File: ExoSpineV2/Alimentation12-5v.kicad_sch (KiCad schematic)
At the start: 8 parts, among them U5 TPS564247

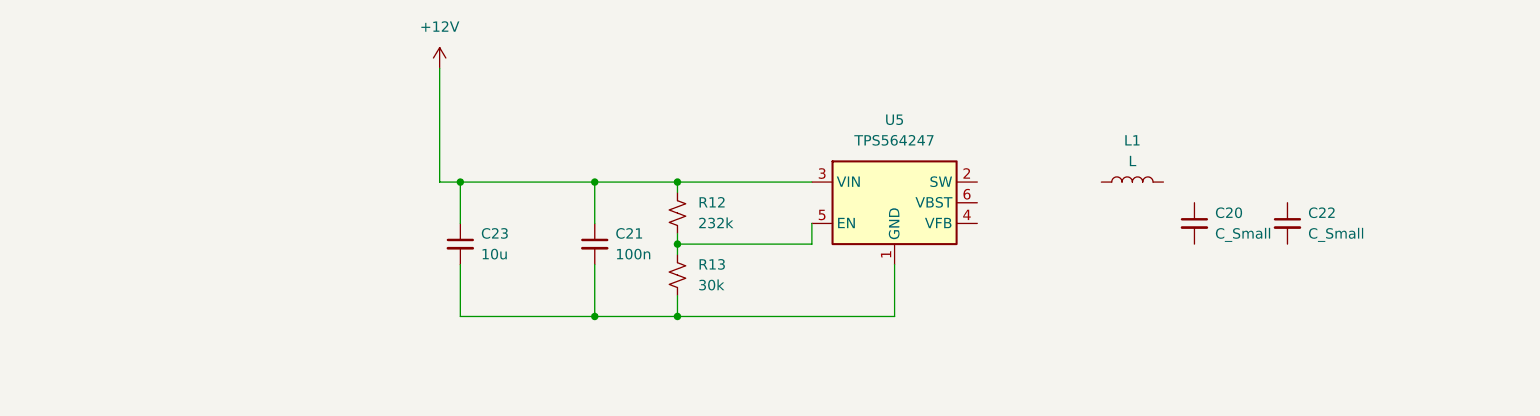
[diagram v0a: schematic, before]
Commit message: ajout des capteurs de pression (x3) et d'un peu d'info sur le dcdc12-5v
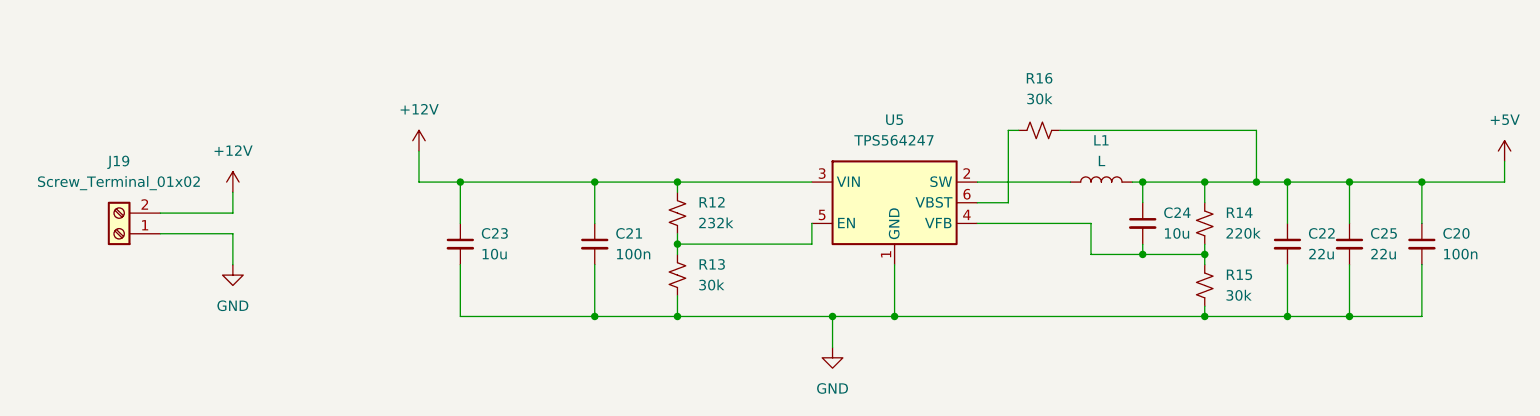
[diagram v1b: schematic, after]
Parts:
- added C24: 10u, symbol Device:C_Small
- added C25: 22u, symbol Device:C_Small
- added J19: Screw_Terminal_01x02, symbol Connector:Screw_Terminal_01x02
- added R14: 220k, symbol Device:R_Small_US
- added R15, R16: 30k, symbol Device:R_Small_US
- C20: value C_Small -> 100n
- C22: value C_Small -> 22u
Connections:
- net +12V: now also J19.2 (Pin_2)
- net +5V: now reaches C22.1
- net +5V: now also C20.1, L1.2, C24.1, C25.1, R14.1, R16.2
- net GND: now reaches C22.2
- net GND: now also C20.2, C21.2, C23.2, R13.2, U5.1 (GND), C25.2, J19.1 (Pin_1), R15.2
- net at U5.2 (SW): now also L1.1
- net at U5.4 (VFB): now also C24.2, R14.2, R15.1
- net at U5.6 (VBST): now also R16.1
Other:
- moved on the sheet: C20, C22, L1

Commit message: jsp ce que j'ai fait mais j'ai avancé
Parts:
- J19: footprint (none) -> TerminalBlock_RND:TerminalBlock_RND_205-00001_1x02_P5.00mm_Horizontal
- L1: value L -> 4.7u
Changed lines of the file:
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@@
       (effects (font (size 1.27 1.27)))
     )
-    (property "Footprint" "" (at 46.99 85.09 0)
+    (property "Footprint" "TerminalBlock_RND:TerminalBlock_RND_205-00001_1x02_P5.00mm_Horizontal" (at 46.99 85.09 0)
       (effects (font (size 1.27 1.27)) hide)
     )
@@
       (effects (font (size 1.27 1.27)) hide)
     )
+    (property "Sim.Enable" "0" (at 142.24 81.28 0)
+      (effects (font (size 1.27 1.27)) hide)
+    )
     (pin "1")
     (pin "2")
@@
       (effects (font (size 1.27 1.27)))
     )
-    (property "Value" "L" (at 167.64 76.2 90)
+    (property "Value" "4.7u" (at 167.64 76.2 90)
       (effects (font (size 1.27 1.27)))
     )
